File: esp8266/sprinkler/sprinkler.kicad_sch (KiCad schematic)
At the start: 27 parts, among them Q1 AO4407A, U1 MAX1873TEEE

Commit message: New sheets
Added power sheet and micro controller sheet
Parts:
- removed C1: 47uF, symbol Device:C_Polarized_US
- removed D1, D2: MBRS340, Diode_SMD:D_SMC, symbol Diode:MBRS340
- removed L1: L, symbol Device:L
- removed Q1: AO4407A, AO4407A:SOIC127P600X175-8N, symbol Alpha_Omega:AO4407A
- removed R1, R2, R3: 100K, symbol Device:R_Small_US
- removed RCCV: 10K, symbol Device:R_US
- removed Rp, Rp1: 4.7, symbol Device:R_Small_US
- removed U1: MAX1873TEEE, Package_SO:QSOP-16_3.9x4.9mm_P0.635mm, symbol Battery_Management:MAX1873TEEE
- removed c1, c2: 0u1F, symbol Device:C_Small
- removed cbatt: 68uF, symbol Device:C_Polarized_US
- removed cccv: 100nf, symbol Device:C_Small
- removed cci, ccs: 47nF, symbol Device:C_Small
- removed ccvp: 1nF, symbol Device:C_Small
- removed cdcin, cvh: 220nF, symbol Device:C_Small
- removed cn, cp: 100nF, symbol Device:C_Small
- removed cref: 1uF, symbol Device:C_Small
- removed cvl: 2u2nF, symbol Device:C_Small
- removed rcsb: 68m, symbol Device:R_Small_US
- removed rcss: 33m, symbol Device:R_Small_US
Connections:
- no-connect marks 1 -> 0
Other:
- added sheet Microcontroller (Microcontroller.kicad_sch)
- added sheet Power Sheet (Power.kicad_sch)

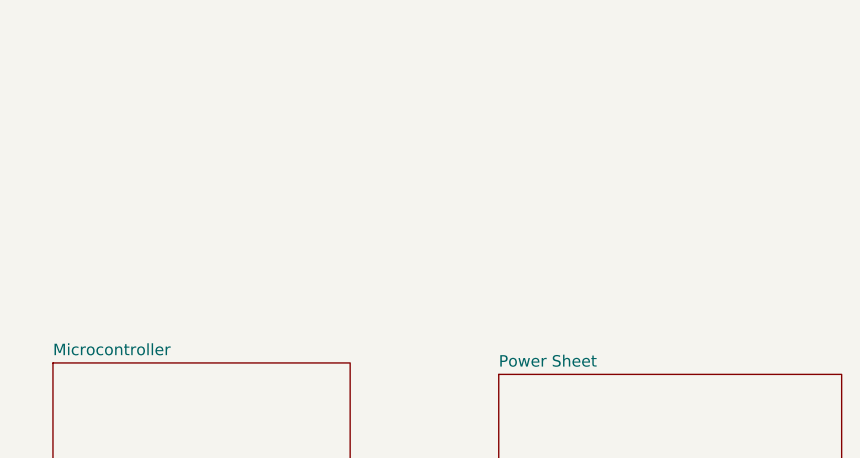
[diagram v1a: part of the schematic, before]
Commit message: Sprinklers
Added RTC and valver drivers modules for the Sprinklers
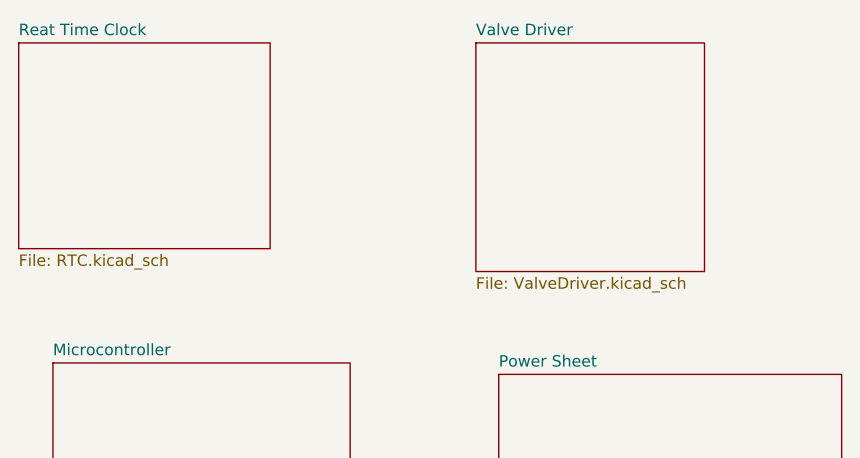
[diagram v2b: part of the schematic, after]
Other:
- added sheet Reat Time Clock (RTC.kicad_sch)
- added sheet Valve Driver (ValveDriver.kicad_sch)
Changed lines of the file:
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@@
+		)
+	)
+	(sheet
+		(at 76.2 50.8)
+		(size 27.94 22.86)
+		(exclude_from_sim no)
+		(in_bom yes)
+		(on_board yes)
+		(dnp no)
+		(fields_autoplaced yes)
+		(stroke
+			(width 0.1524)
+			(type solid)
+		)
+		(fill
+			(color 0 0 0 0.0000)
+		)
+		(property "Sheetname" "Reat Time Clock"
+			(at 76.2 50.0884 0)
+			(effects
+				(font
+					(size 1.27 1.27)
+				)
+				(justify left bottom)
+			)
+		)
+		(property "Sheetfile" "RTC.kicad_sch"
+			(at 76.2 74.2446 0)
+			(effects
+				(font
+					(size 1.27 1.27)
+				)
+				(justify left top)
+			)
+		)
+		(instances
+			(project "sprinkler"
+				(path "/00ed8740-45a2-4b9d-9104-9548b81da339"
+					(page "4")
+				)
+			)
+		)
+	)
+	(sheet
+		(at 127 50.8)
+		(size 25.4 25.4)
+		(exclude_from_sim no)
+		(in_bom yes)
+		(on_board yes)
+		(dnp no)
+		(fields_autoplaced yes)
+		(stroke
+			(width 0.1524)
+			(type solid)
+		)
+		(fill
+			(color 0 0 0 0.0000)
+		)
+		(property "Sheetname" "Valve Driver"
+			(at 127 50.0884 0)
+			(effects
+				(font
+					(size 1.27 1.27)
+				)
+				(justify left bottom)
+			)
+		)
+		(property "Sheetfile" "ValveDriver.kicad_sch"
+			(at 127 76.7846 0)
+			(effects
+				(font
+					(size 1.27 1.27)
+				)
+				(justify left top)
+			)
+		)
+		(instances
+			(project "sprinkler"
+				(path "/00ed8740-45a2-4b9d-9104-9548b81da339"
+					(page "5")
+				)
+			)
 		)
 	)

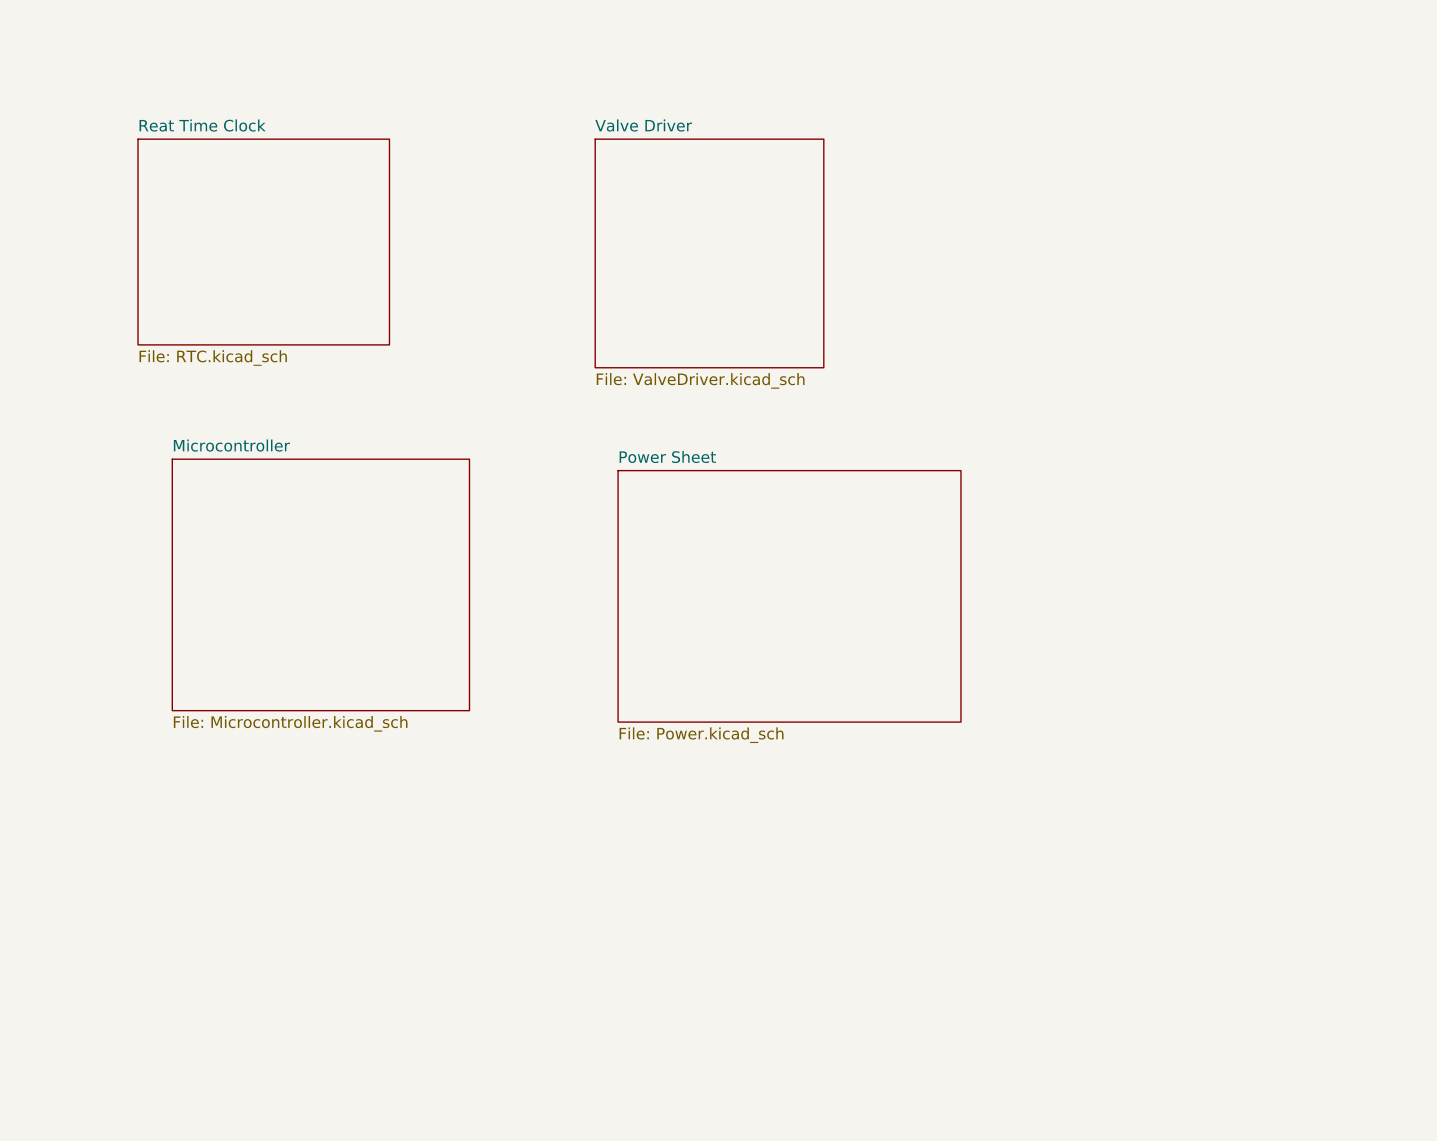
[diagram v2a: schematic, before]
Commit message: Update connections
Connect Micro controller inputs and outputs
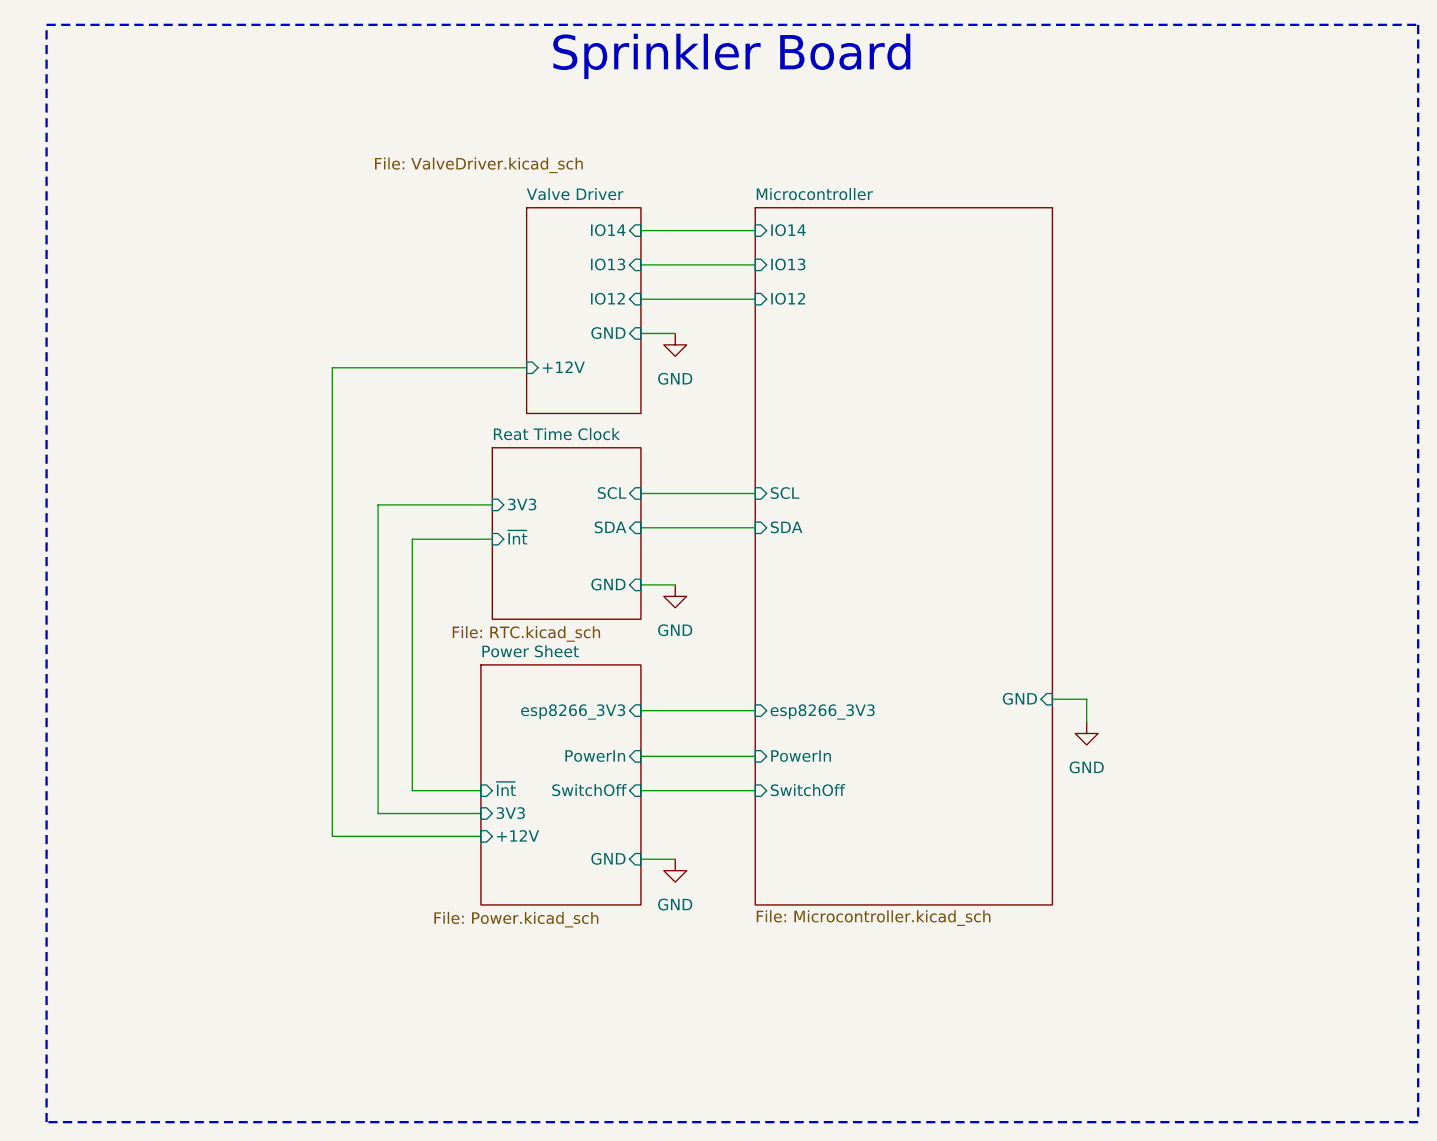
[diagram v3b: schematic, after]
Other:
- sheet Microcontroller ports: added GND, IO12, IO13, IO14, PowerIn, SCL, SDA, SwitchOff, esp8266_3V3; removed none
- sheet Power Sheet ports: added +12V, 3V3, GND, PowerIn, SwitchOff, esp8266_3V3, ~{Int}; removed none
- sheet Reat Time Clock ports: added 3V3, GND, SCL, SDA, ~{Int}; removed none
- sheet Valve Driver ports: added +12V, GND, IO12, IO13, IO14; removed none
